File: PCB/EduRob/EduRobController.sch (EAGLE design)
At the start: 31 parts, among them J1 665306124022, J2 665306124022, M3 665306124022, M4 665306124022

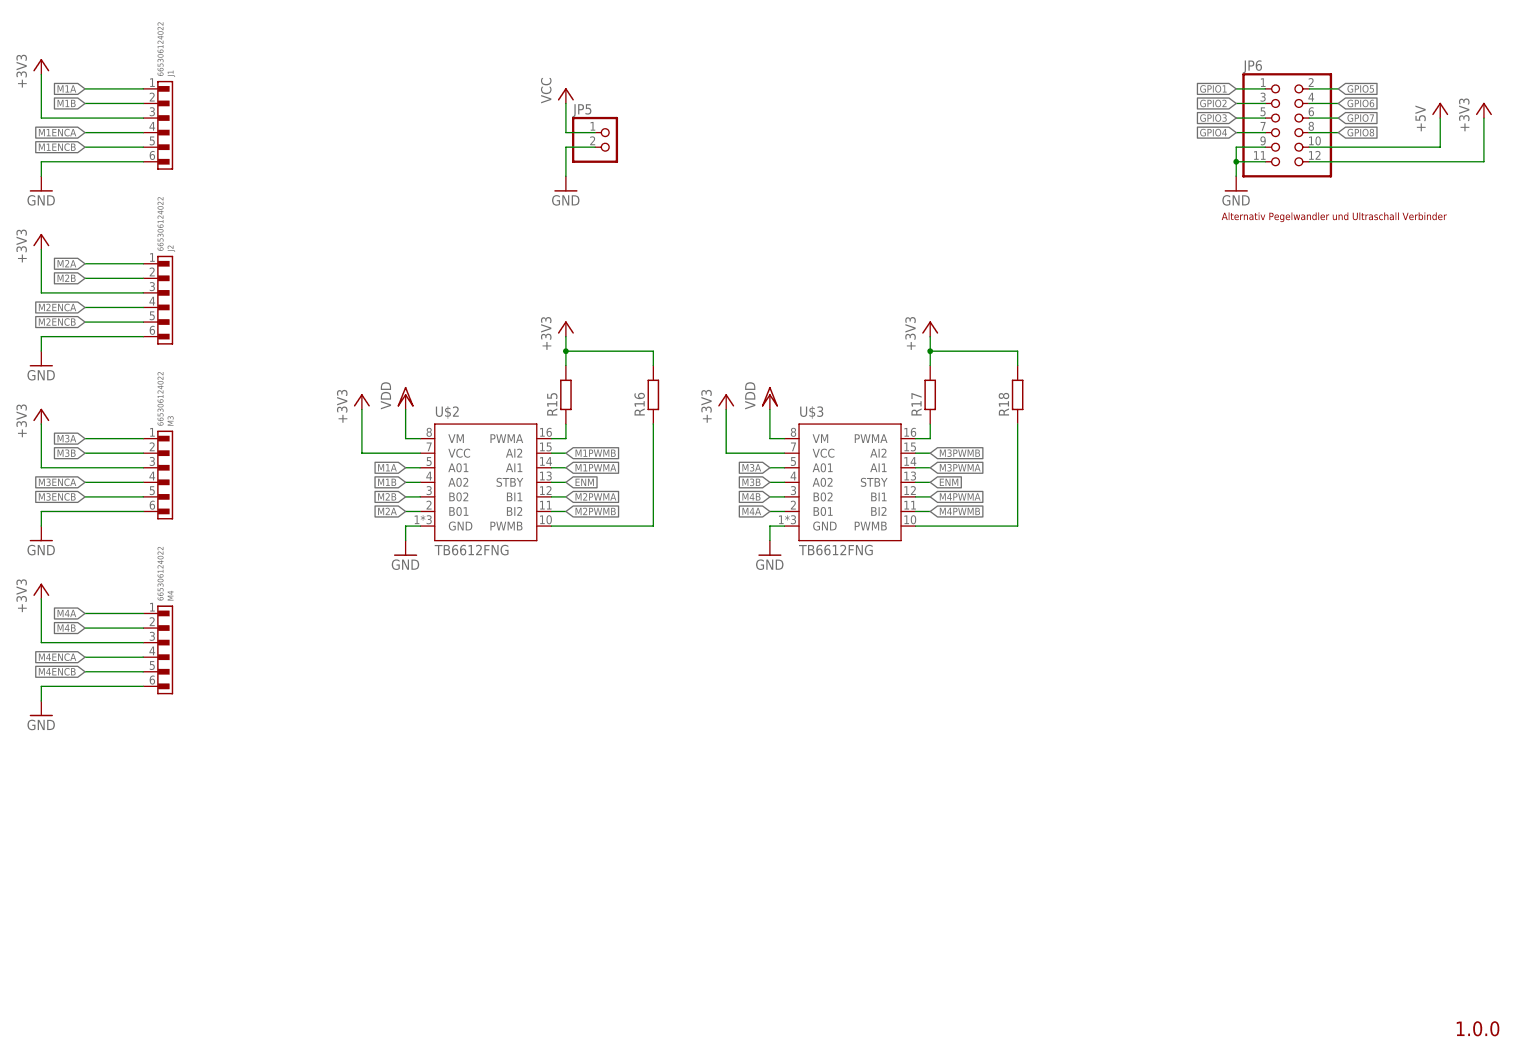
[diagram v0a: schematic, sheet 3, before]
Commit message: New Connectors and minor changes
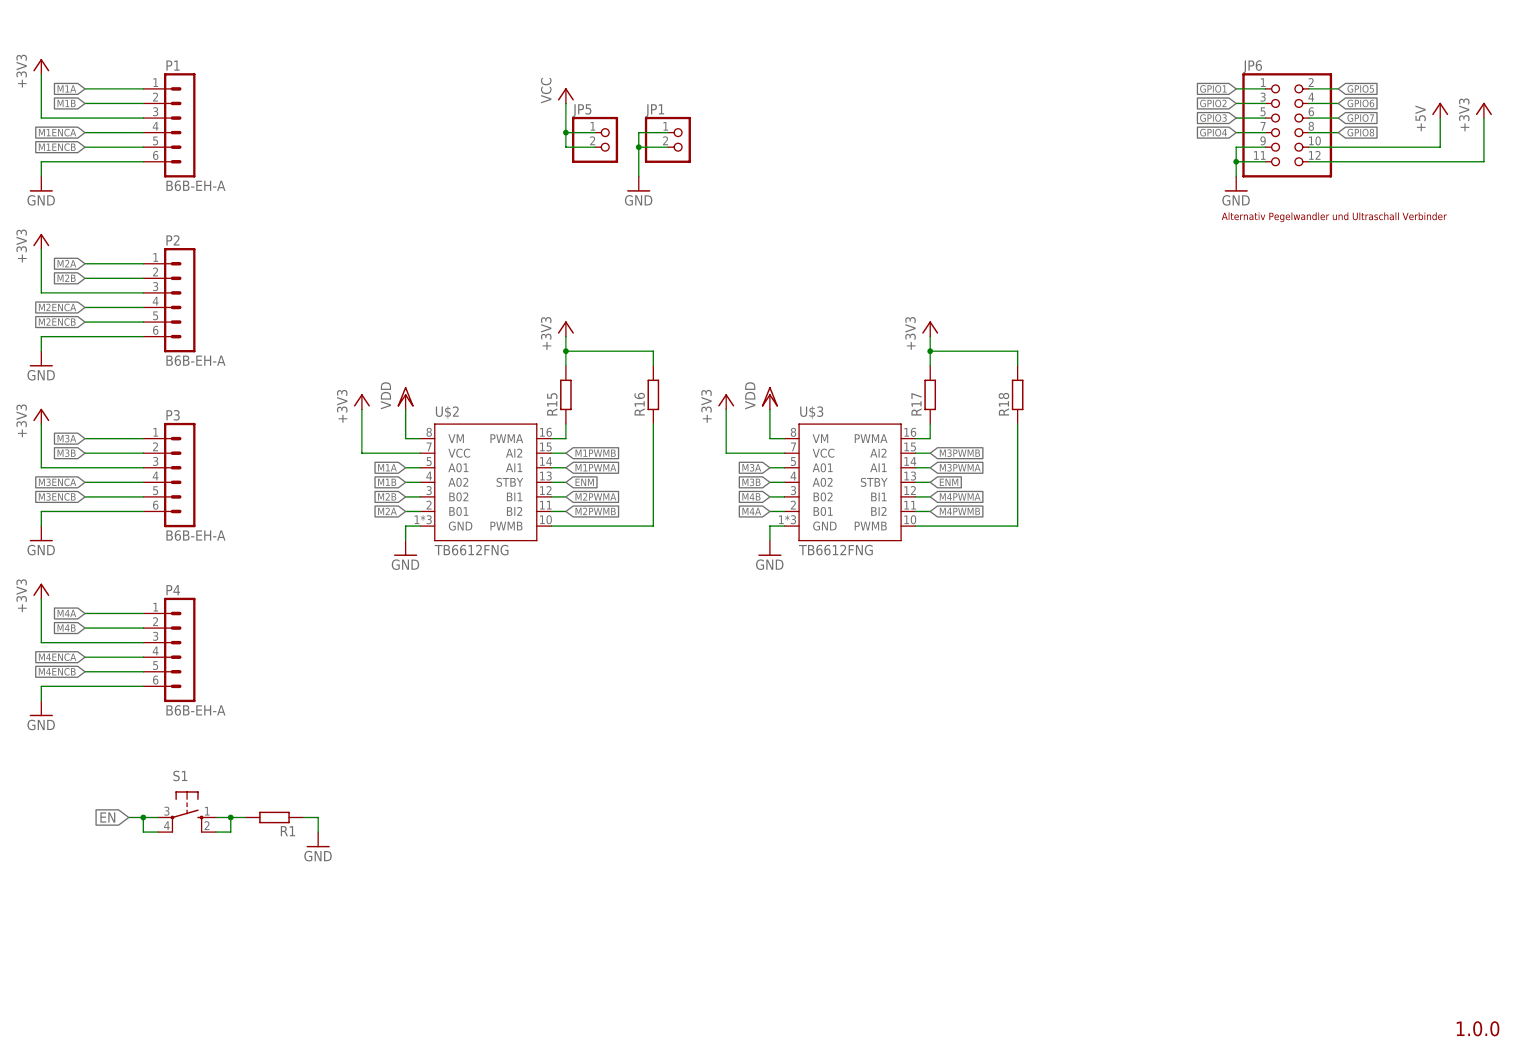
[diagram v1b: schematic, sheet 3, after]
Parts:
- removed J1, J2, M3, M4: 665306124022, Wurth_Connectors_WR-WTB:665306124022
- added JP1: (no value), pinhead:PINHD-1X2
- added P1, P2, P3, P4: B6B-EH-A, con-jst-eh:B6B-EH-A
- added R1: (no value), rcl:R-EU_R0603
- added S1: (no value), switch-omron:10-XX
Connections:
- new net N$2: R1.2, S1.S, S1.S1
- net +3V3: now also P1.3, P2.3, P3.3, P4.3; no longer J1.3, J2.3, M3.3, M4.3
- net EN: now also S1.P, S1.P1
- net GND: now also JP1.1, JP1.2, P1.6, P2.6, P3.6, P4.6, R1.1; no longer J1.6, J2.6, JP5.2, M3.6, M4.6
- net M1A: now also P1.1; no longer J1.1
- net M1B: now also P1.2; no longer J1.2
- net M1ENCA: now also P1.4; no longer J1.4
- net M1ENCB: now also P1.5; no longer J1.5
- net M2A: now also P2.1; no longer J2.1
- net M2B: now also P2.2; no longer J2.2
- net M2ENCA: now also P2.4; no longer J2.4
- net M2ENCB: now also P2.5; no longer J2.5
- net M3A: now also P3.1; no longer M3.1
- net M3B: now also P3.2; no longer M3.2
- net M3ENCA: now also P3.4; no longer M3.4
- net M3ENCB: now also P3.5; no longer M3.5
- net M4A: now also P4.1; no longer M4.1
- net M4B: now also P4.2; no longer M4.2
- net M4ENCA: now also P4.4; no longer M4.4
- net M4ENCB: now also P4.5; no longer M4.5
- net VCC: now also JP5.2
